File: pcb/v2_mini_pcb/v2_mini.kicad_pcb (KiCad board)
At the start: 6 copper layers, 60.8 x 35.1 mm, 118 parts, among them J1 Conn_Coaxial, J2 GTFP08441BEU, J3 SFV24R-2STE1HLF, J5 TC2030, J6 USB4105-GF-A, Q1 NTNS3164NZT5G, SW1 SW_Push, SW2 SW_Push, SW3 SW_Push, SW4 SW_Push, SW5 SW_Push, SW6 SW_Push, SW7 SW_Push, U1 UM980, U10 TPS63802DLAR, U3 SCH16T-K01-1, U4 LP5813ADRRR, U5 TCA9536ADTMR, U6 TPD4EUSB30, U7 MAX16169AALTA+T, U8 BQ25622ERYKR, U9 MAX17048G_T10

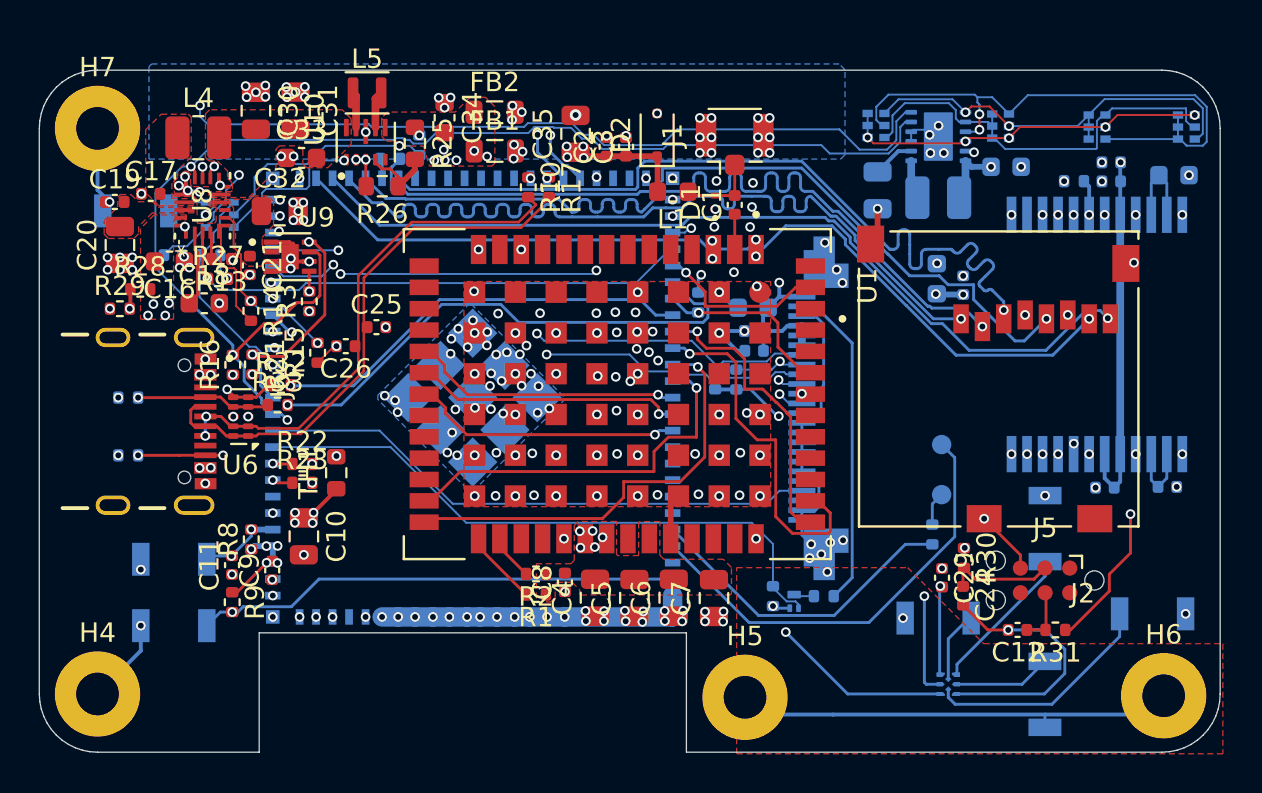
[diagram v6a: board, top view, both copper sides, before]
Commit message: keepout antenna
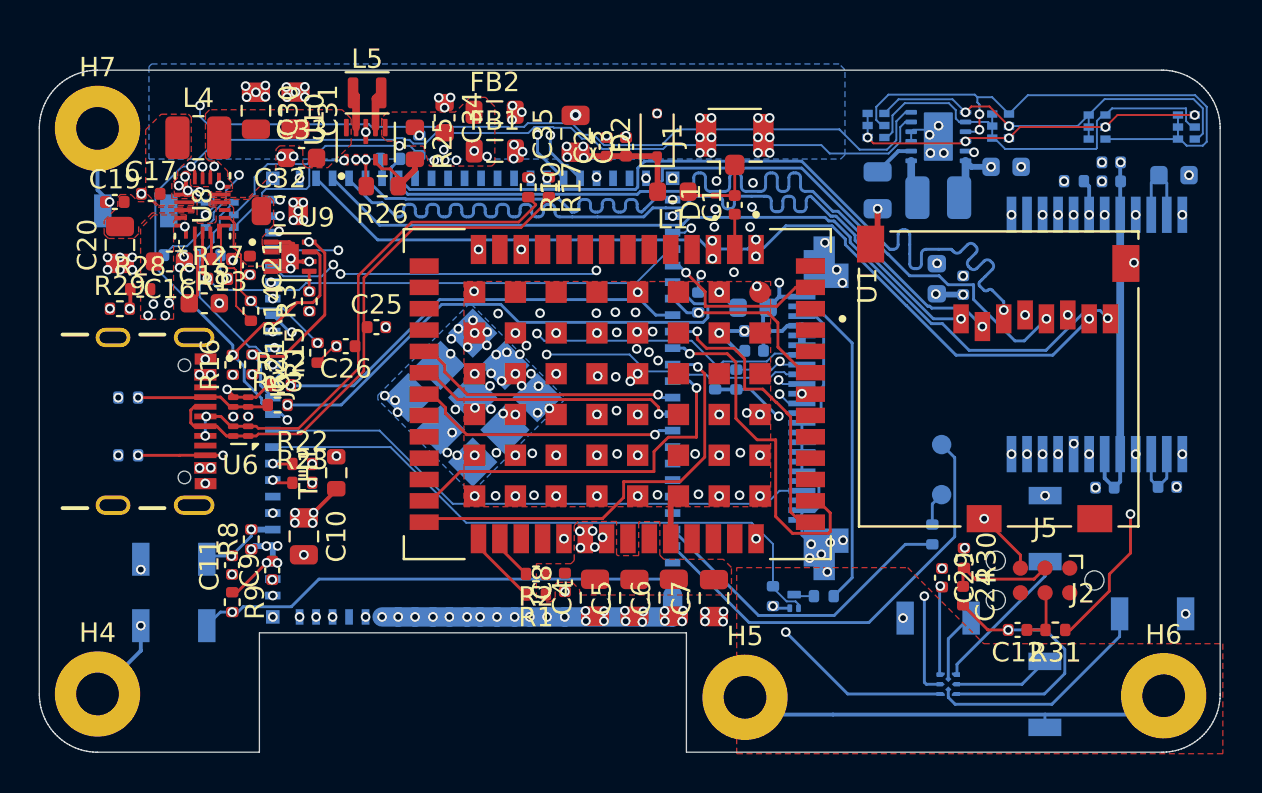
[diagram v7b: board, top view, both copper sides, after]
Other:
- outline, holes or cut-outs redrawn
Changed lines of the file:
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@@
 	(gr_poly
 		(pts
-			(xy 86.67 113.77) (xy 86.67 107.62) (xy 108.68 107.62) (xy 108.68 113.77)
-			(arc
-				(start 133.18 113.77)
-				(mid 135.30132 112.89132)
-				(end 136.18 110.77)
-			)
-			(arc
-				(start 136.18 81.63)
-				(mid 135.30132 79.50868)
-				(end 133.18 78.63)
-			)
-			(arc
-				(start 78.34 78.63)
-				(mid 76.21868 79.50868)
-				(end 75.34 81.63)
-			)
-			(arc
-				(start 75.34 110.77)
-				(mid 76.21868 112.89132)
-				(end 78.34 113.77)
-			)
+			(xy 86.68 113.77) (xy 86.68 107.62) (xy 108.68 107.62) (xy 108.68 113.77) (xy 133.18 113.77) (xy 133.258544 113.769486)
+			(xy 133.415418 113.761264) (xy 133.571646 113.744844) (xy 133.7268 113.72027) (xy 133.880456 113.68761)
+			(xy 134.032192 113.646952) (xy 134.181592 113.598409) (xy 134.328247 113.542113) (xy 134.471755 113.47822)
+			(xy 134.611722 113.406903) (xy 134.747764 113.328359) (xy 134.87951 113.242802) (xy 135.006597 113.150468)
+			(xy 135.128678 113.051609) (xy 135.245418 112.946496) (xy 135.356496 112.835418) (xy 135.461609 112.718678)
+			(xy 135.560468 112.596597) (xy 135.652802 112.46951) (xy 135.738359 112.337764) (xy 135.816903 112.201722)
+			(xy 135.88822 112.061755) (xy 135.952113 111.918247) (xy 136.008409 111.771592) (xy 136.056952 111.622192)
+			(xy 136.09761 111.470456) (xy 136.13027 111.3168) (xy 136.154844 111.161646) (xy 136.171264 111.005418)
+			(xy 136.179486 110.848544) (xy 136.18 110.77) (xy 136.18 81.63) (xy 136.179486 81.551456) (xy 136.171264 81.394582)
+			(xy 136.154844 81.238354) (xy 136.13027 81.0832) (xy 136.09761 80.929544) (xy 136.056952 80.777808)
+			(xy 136.008409 80.628408) (xy 135.952113 80.481753) (xy 135.88822 80.338245) (xy 135.816903 80.198278)
+			(xy 135.738359 80.062236) (xy 135.652802 79.93049) (xy 135.560468 79.803403) (xy 135.461609 79.681322)
+			(xy 135.356496 79.564582) (xy 135.245418 79.453504) (xy 135.128678 79.348391) (xy 135.006597 79.249532)
+			(xy 134.87951 79.157198) (xy 134.747764 79.071641) (xy 134.611722 78.993097) (xy 134.471755 78.92178)
+			(xy 134.328247 78.857887) (xy 134.181592 78.801591) (xy 134.032192 78.753048) (xy 133.880456 78.71239)
+			(xy 133.7268 78.67973) (xy 133.571646 78.655156) (xy 133.415418 78.638736) (xy 133.258544 78.630514)
+			(xy 133.18 78.63) (xy 78.34 78.63) (xy 78.261456 78.630514) (xy 78.104582 78.638736) (xy 77.948354 78.655156)
+			(xy 77.7932 78.67973) (xy 77.639544 78.71239) (xy 77.487808 78.753048) (xy 77.338408 78.801591) (xy 77.191753 78.857887)
+			(xy 77.048245 78.92178) (xy 76.908278 78.993097) (xy 76.772236 79.071641) (xy 76.64049 79.157198)
+			(xy 76.513403 79.249532) (xy 76.391322 79.348391) (xy 76.274582 79.453504) (xy 76.163504 79.564582)
+			(xy 76.058391 79.681322) (xy 75.959532 79.803403) (xy 75.867198 79.93049) (xy 75.781641 80.062236)
+			(xy 75.703097 80.198278) (xy 75.63178 80.338245) (xy 75.567887 80.481753) (xy 75.511591 80.628408)
+			(xy 75.463048 80.777808) (xy 75.42239 80.929544) (xy 75.38973 81.0832) (xy 75.365156 81.238354) (xy 75.348736 81.394582)
+			(xy 75.340514 81.551456) (xy 75.34 81.63) (xy 75.34 110.77) (xy 75.340514 110.848544) (xy 75.348736 111.005418)
+			(xy 75.365156 111.161646) (xy 75.38973 111.3168) (xy 75.42239 111.470456) (xy 75.463048 111.622192)
+			(xy 75.511591 111.771592) (xy 75.567887 111.918247) (xy 75.63178 112.061755) (xy 75.703097 112.201722)
+			(xy 75.781641 112.337764) (xy 75.867198 112.46951) (xy 75.959532 112.596597) (xy 76.058391 112.718678)
+			(xy 76.163504 112.835418) (xy 76.274582 112.946496) (xy 76.391322 113.051609) (xy 76.513403 113.150468)
+			(xy 76.64049 113.242802) (xy 76.772236 113.328359) (xy 76.908278 113.406903) (xy 77.048245 113.47822)
+			(xy 77.191753 113.542113) (xy 77.338408 113.598409) (xy 77.487808 113.646952) (xy 77.639544 113.68761)
+			(xy 77.7932 113.72027) (xy 77.948354 113.744844) (xy 78.104582 113.761264) (xy 78.261456 113.769486)
+			(xy 78.34 113.77)
 		)
 		(stroke
@@
 			)
 		)
+	)
+	(zone
+		(layers "F.Cu" "B.Cu" "In1.Cu" "In2.Cu" "In3.Cu" "In4.Cu")
+		(name "keepout")
+		(hatch edge 0.5)
+		(connect_pads yes
+			(clearance 0)
+		)
+		(min_thickness 0.2)
+		(keepout
+			(tracks not_allowed)
+			(vias not_allowed)
+			(pads not_allowed)
+			(copperpour not_allowed)
+			(footprints not_allowed)
+		)
+		(placement
+			(enabled no)
+			(sheetname "/ESP32-S31 MCU/")
+		)
+		(fill
+			(thermal_gap 0.5)
+			(thermal_bridge_width 0.5)
+			(island_removal_mode 0)
+		)
+		(polygon
+			(pts
+				(xy 86.7 113.85) (xy 86.7 107.59) (xy 108.65 107.59) (xy 108.68 107.62) (xy 108.68 113.85)
+			)
+		)

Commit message: better length tuning
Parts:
- moved C28 0.36 mm to (118.7, 84.5)
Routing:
- net Net-(J2-CLK): track 41.2 -> 44.2 mm
- net /ESP32-S31 MCU/SD_CMD: track 42.9 -> 44.7 mm
